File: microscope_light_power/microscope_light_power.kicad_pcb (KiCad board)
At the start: 2 copper layers, 50 x 40 mm, 36 parts, among them IC1 TPS61090, J1 MICROUSB, J2 5V175_out, J3 enable_switch, U1 MCP73871-2AA

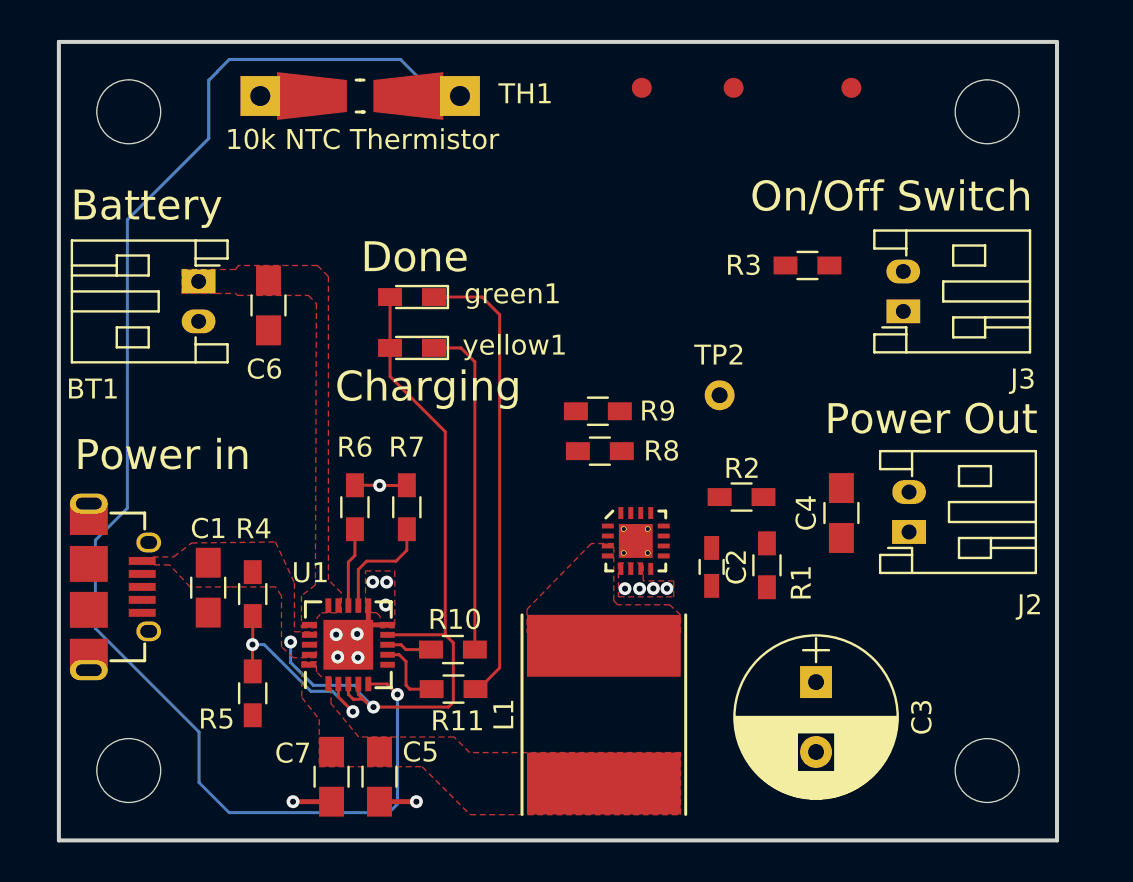
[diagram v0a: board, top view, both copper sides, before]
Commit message: Routed everything connected to the TPS61090. Also routed the test points and connectors. Only thing left is ground!
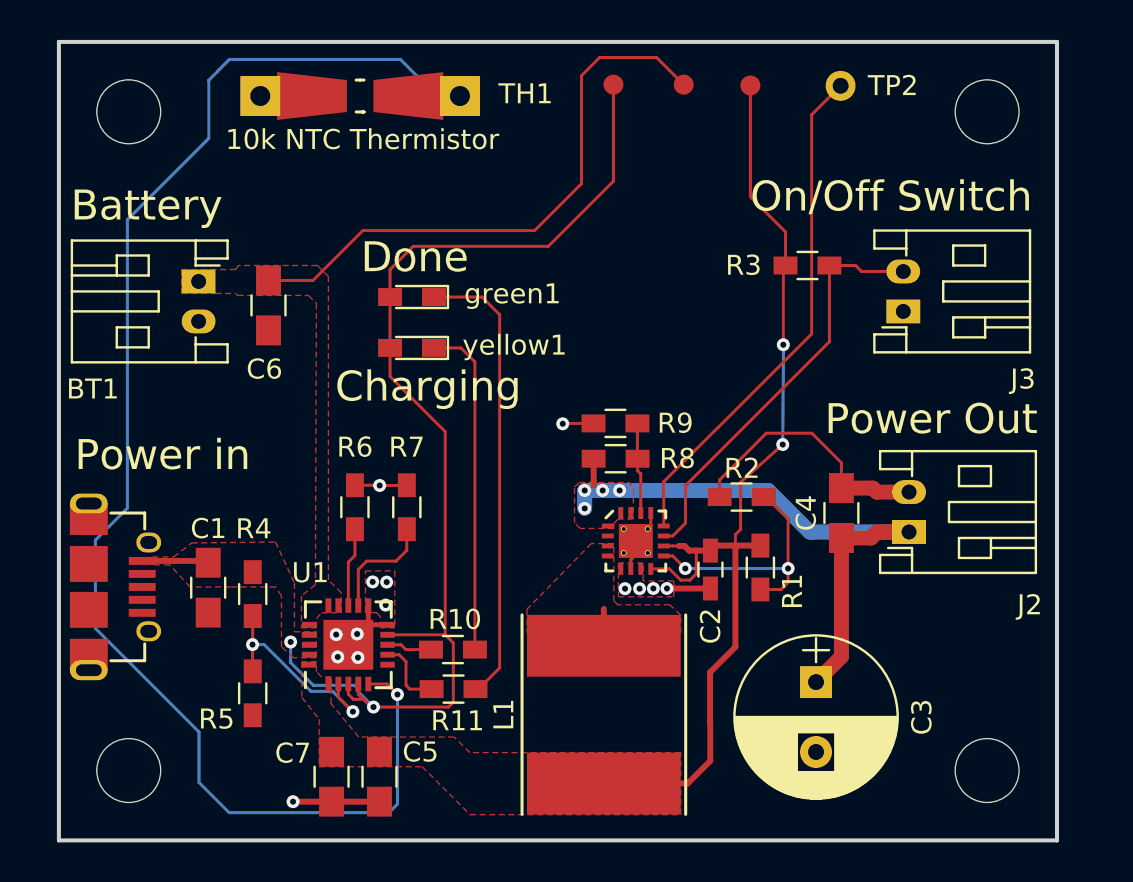
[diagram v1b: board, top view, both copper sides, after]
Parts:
- moved TP2 16.6 mm to (139.2, 122.2)
- moved TP4 5.06 mm to (134.6, 122.2)
- moved TP3 2.51 mm to (131.3, 122.1)
- moved TP1 1.43 mm to (127.8, 122.1)
- moved R9 1.07 mm to (127.9, 139.1)
- moved R8 0.88 mm to (127.9, 140.9)
- moved R1 0.35 mm to (135.1, 146.3), turned to 270 degrees
- moved C2 0.14 mm to (132.6, 146.4)
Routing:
- net /Vout: track 0.00 -> 50.9 mm, vias 0 -> 2
- net /5V175: track 0.00 -> 30.6 mm, vias 0 -> 4
- net /Vbat: track 0.00 -> 29.2 mm
- net /low_battery: track 0.00 -> 25.7 mm
- net /Vusb: track 37.7 -> 60.3 mm
- net GND: track 8.85 -> 31.4 mm
- net /enable: track 0.00 -> 21.1 mm
- net Net-(IC1-Pad9): track 0.00 -> 12.9 mm, vias 0 -> 2
- net Net-(IC1-Pad14): track 0.00 -> 4.56 mm
- net Net-(TH1-Pad1): track 71.4 -> 74.0 mm
- net /SW: track 0.00 -> 1.85 mm
- added copper zone on F.Cu, net /5V175

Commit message: Change the TPS61090 annotation from IC* to U* and move the reference designator on to the silkscreen layer.
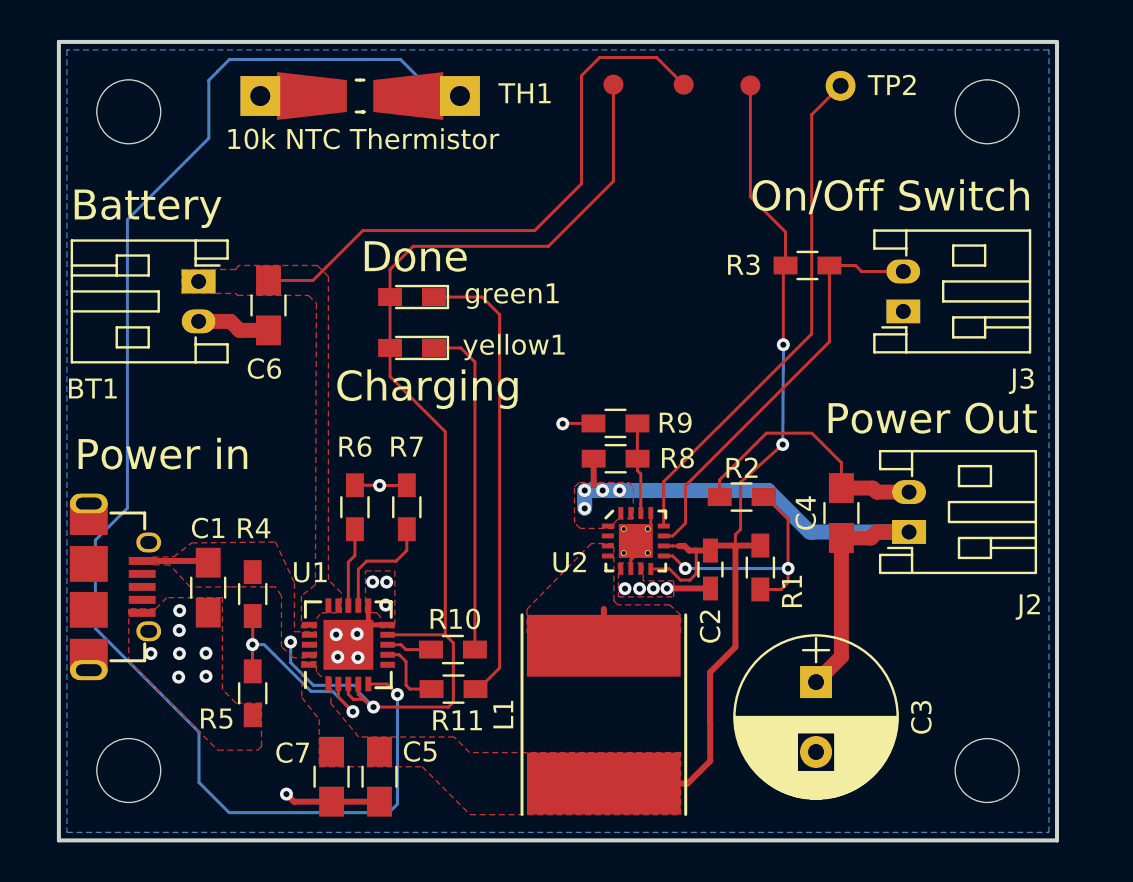
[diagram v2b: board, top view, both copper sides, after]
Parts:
- renumbered IC1 to U2
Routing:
- net GND: track 31.4 -> 35.5 mm, vias 14 -> 21
- added copper zone on B.Cu, net GND
